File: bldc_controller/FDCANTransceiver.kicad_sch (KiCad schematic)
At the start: 4 parts, among them U9 TCAN1057AEVDRQ1

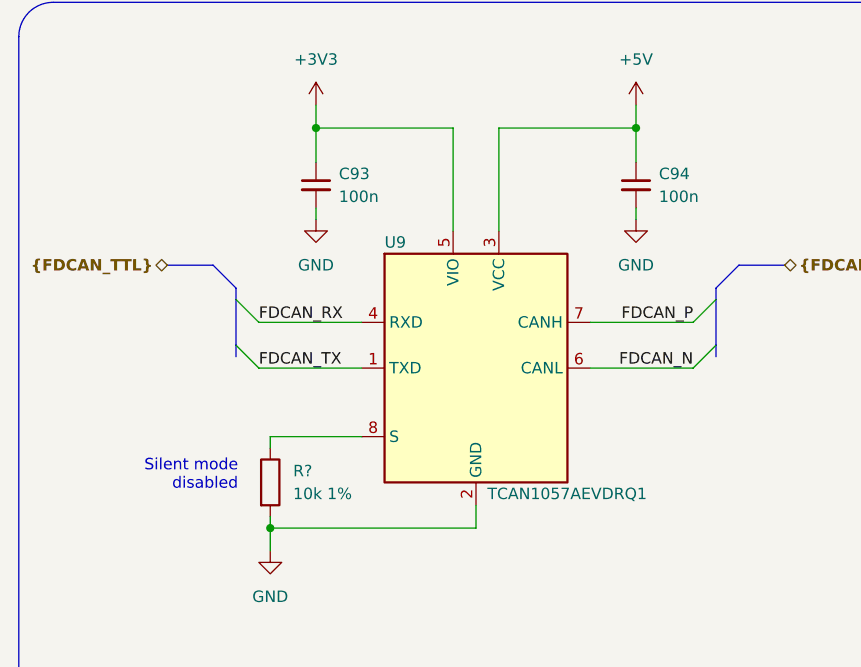
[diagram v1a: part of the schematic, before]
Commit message: added IPC-7351 compliant footprints and started routing
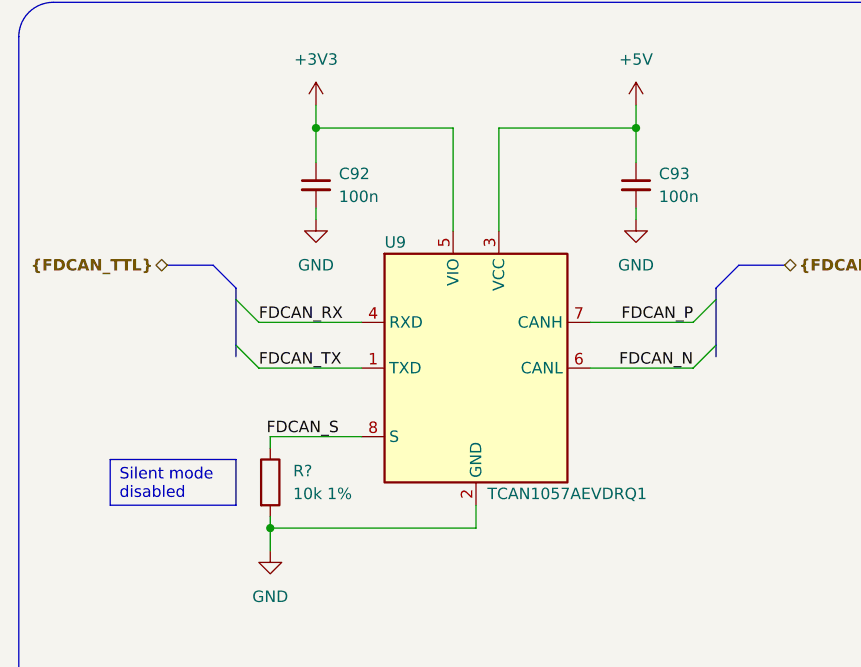
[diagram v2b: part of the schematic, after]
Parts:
- C92: renamed from C93; footprint Capacitor_SMD:C_0402_1005Metric -> 0_capacitor_smd:C_0402_1005_DensityHigh
- C93: renamed from C94; footprint Capacitor_SMD:C_0402_1005Metric -> 0_capacitor_smd:C_0402_1005_DensityHigh
- R?: footprint Resistor_SMD:R_0402_1005Metric -> 0_resistor_smd:R_0402_1005_DensityHigh
- U9: footprint Package_SO:SOIC-8-N7_3.9x4.9mm_P1.27mm -> Package_SO:SOIC-8_3.9x4.9mm_P1.27mm
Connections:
- net FDCAN_S: now reaches R?.1, U9.8 (S)
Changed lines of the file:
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@@
+    (stroke (width 0) (type default))
+  )
+  (wire (pts (xy 127 100.33) (xy 137.16 100.33))
     (stroke (width 0) (type default))
   )
@@
     (stroke (width 0) (type default))
   )
-  (wire (pts (xy 127 100.33) (xy 137.16 100.33))
-    (stroke (width 0) (type default))
-  )
   (wire (pts (xy 147.32 66.04) (xy 147.32 77.47))
     (stroke (width 0) (type default))
@@
     (stroke (width 0) (type default))
     (fill (type none))
-  )
-  (text_box "Silent mode disabled"
-    (at 110.49 101.6 0) (size 13.97 6.35)
-    (stroke (width -0.0001) (type default))
-    (fill (type none))
-    (effects (font (size 1.27 1.27)) (justify right top))
   )
   (text_box "Back to Top Level"
@@
     (effects (font (size 2.54 2.54) (color 0 0 0 1)) (justify bottom))
   )
+  (text_box "Silent mode disabled"
+    (at 109.22 102.87 0) (size 13.97 5.08)
+    (stroke (width 0) (type default) (color 0 0 0 1))
+    (fill (type color) (color 191 240 255 1))
+    (effects (font (size 1.27 1.27) (color 0 0 0 1)) (justify left))
+  )
+  (label "FDCAN_S" (at 134.62 100.33 180) (fields_autoplaced)
+    (effects (font (size 1.27 1.27)) (justify right bottom))
+  )
   (label "FDCAN_P" (at 173.99 87.63 180) (fields_autoplaced)
     (effects (font (size 1.27 1.27)) (justify right bottom))
@@
   (symbol (lib_id "power:+3V3") (at 132.08 63.5 0) (unit 1)
     (in_bom yes) (on_board yes) (dnp no) (fields_autoplaced)
-    (property "Reference" "#PWR054" (at 132.08 67.31 0)
+    (property "Reference" "#PWR053" (at 132.08 67.31 0)
       (effects (font (size 1.27 1.27)) hide)
     )
@@
       (project "bldc_controller"
         (path "/0650c7a8-acba-429c-9f8e-eec0baf0bc1c/926acdff-90be-4f7b-9e19-9f96ee9f0571"
+          (reference "#PWR053") (unit 1)
+        )
+      )
+    )
+  )
+  (symbol (lib_id "power:GND") (at 127 113.03 0) (unit 1)
+    (in_bom yes) (on_board yes) (dnp no) (fields_autoplaced)
+    (property "Reference" "#PWR052" (at 127 119.38 0)
+      (effects (font (size 1.27 1.27)) hide)
+    )
+    (property "Value" "GND" (at 127 118.11 0)
+      (effects (font (size 1.27 1.27)))
+    )
+    (property "Footprint" "" (at 127 113.03 0)
+      (effects (font (size 1.27 1.27)) hide)
+    )
+    (property "Datasheet" "" (at 127 113.03 0)
+      (effects (font (size 1.27 1.27)) hide)
+    )
+    (pin "1")
+    (instances
+      (project "bldc_controller"
+        (path "/0650c7a8-acba-429c-9f8e-eec0baf0bc1c/926acdff-90be-4f7b-9e19-9f96ee9f0571"
+          (reference "#PWR052") (unit 1)
+        )
+      )
+    )
+  )
+  (symbol (lib_id "power:GND") (at 132.08 76.2 0) (unit 1)
+    (in_bom yes) (on_board yes) (dnp no) (fields_autoplaced)
+    (property "Reference" "#PWR054" (at 132.08 82.55 0)
+      (effects (font (size 1.27 1.27)) hide)
+    )
+    (property "Value" "GND" (at 132.08 81.28 0)
+      (effects (font (size 1.27 1.27)))
+    )
+    (property "Footprint" "" (at 132.08 76.2 0)
+      (effects (font (size 1.27 1.27)) hide)
+    )
+    (property "Datasheet" "" (at 132.08 76.2 0)
+      (effects (font (size 1.27 1.27)) hide)
+    )
+    (pin "1")
+    (instances
+      (project "bldc_controller"
+        (path "/0650c7a8-acba-429c-9f8e-eec0baf0bc1c/926acdff-90be-4f7b-9e19-9f96ee9f0571"
           (reference "#PWR054") (unit 1)
         )
@@
     )
   )
-  (symbol (lib_id "power:GND") (at 127 113.03 0) (unit 1)
-    (in_bom yes) (on_board yes) (dnp no) (fields_autoplaced)
-    (property "Reference" "#PWR053" (at 127 119.38 0)
-      (effects (font (size 1.27 1.27)) hide)
-    )
-    (property "Value" "GND" (at 127 118.11 0)
-      (effects (font (size 1.27 1.27)))
-    )
-    (property "Footprint" "" (at 127 113.03 0)
-      (effects (font (size 1.27 1.27)) hide)
-    )
-    (property "Datasheet" "" (at 127 113.03 0)
-      (effects (font (size 1.27 1.27)) hide)
-    )
-    (pin "1")
-    (instances
-      (project "bldc_controller"
-        (path "/0650c7a8-acba-429c-9f8e-eec0baf0bc1c/926acdff-90be-4f7b-9e19-9f96ee9f0571"
-          (reference "#PWR053") (unit 1)
-        )
-      )
-    )
-  )
-  (symbol (lib_id "power:GND") (at 132.08 76.2 0) (unit 1)
-    (in_bom yes) (on_board yes) (dnp no) (fields_autoplaced)
-    (property "Reference" "#PWR055" (at 132.08 82.55 0)
-      (effects (font (size 1.27 1.27)) hide)
-    )
-    (property "Value" "GND" (at 132.08 81.28 0)
-      (effects (font (size 1.27 1.27)))
-    )
-    (property "Footprint" "" (at 132.08 76.2 0)
-      (effects (font (size 1.27 1.27)) hide)
-    )
-    (property "Datasheet" "" (at 132.08 76.2 0)
-      (effects (font (size 1.27 1.27)) hide)
-    )
-    (pin "1")
-    (instances
-      (project "bldc_controller"
-        (path "/0650c7a8-acba-429c-9f8e-eec0baf0bc1c/926acdff-90be-4f7b-9e19-9f96ee9f0571"
-          (reference "#PWR055") (unit 1)
-        )
-      )
-    )
-  )
   (symbol (lib_id "power:GND") (at 167.64 76.2 0) (mirror y) (unit 1)
     (in_bom yes) (on_board yes) (dnp no) (fields_autoplaced)
-    (property "Reference" "#PWR057" (at 167.64 82.55 0)
+    (property "Reference" "#PWR056" (at 167.64 82.55 0)
       (effects (font (size 1.27 1.27)) hide)
     )
@@
       (project "bldc_controller"
         (path "/0650c7a8-acba-429c-9f8e-eec0baf0bc1c/926acdff-90be-4f7b-9e19-9f96ee9f0571"
-          (reference "#PWR057") (unit 1)
+          (reference "#PWR056") (unit 1)
         )
       )
@@
   (symbol (lib_id "Device:C_Small") (at 167.64 72.39 0) (unit 1)
     (in_bom yes) (on_board yes) (dnp no)
-    (property "Reference" "C94" (at 170.18 71.1263 0)
+    (property "Reference" "C93" (at 170.18 71.1263 0)
       (effects (font (size 1.27 1.27)) (justify left))
     )
@@
       (effects (font (size 1.27 1.27)) (justify left))
     )
-    (property "Footprint" "Capacitor_SMD:C_0402_1005Metric" (at 167.64 72.39 0)
+    (property "Footprint" "0_capacitor_smd:C_0402_1005_DensityHigh" (at 167.64 72.39 0)
       (effects (font (size 1.27 1.27)) hide)
     )
@@
       (project "bldc_controller"
         (path "/0650c7a8-acba-429c-9f8e-eec0baf0bc1c/926acdff-90be-4f7b-9e19-9f96ee9f0571"
-          (reference "C94") (unit 1)
+          (reference "C93") (unit 1)
         )
       )
@@
   (symbol (lib_id "power:+5V") (at 167.64 63.5 0) (unit 1)
     (in_bom yes) (on_board yes) (dnp no) (fields_autoplaced)
-    (property "Reference" "#PWR056" (at 167.64 67.31 0)
+    (property "Reference" "#PWR055" (at 167.64 67.31 0)
       (effects (font (size 1.27 1.27)) hide)
     )
@@
       (project "bldc_controller"
         (path "/0650c7a8-acba-429c-9f8e-eec0baf0bc1c/926acdff-90be-4f7b-9e19-9f96ee9f0571"
-          (reference "#PWR056") (unit 1)
+          (reference "#PWR055") (unit 1)
         )
       )
@@
       (effects (font (size 1.27 1.27)) (justify left))
     )
-    (property "Footprint" "Package_SO:SOIC-8-N7_3.9x4.9mm_P1.27mm" (at 149.86 116.84 0)
+    (property "Footprint" "Package_SO:SOIC-8_3.9x4.9mm_P1.27mm" (at 149.86 116.84 0)
       (effects (font (size 1.27 1.27)) hide)
     )
@@
   (symbol (lib_id "Device:C_Small") (at 132.08 72.39 0) (unit 1)
     (in_bom yes) (on_board yes) (dnp no) (fields_autoplaced)
-    (property "Reference" "C93" (at 134.62 71.1263 0)
+    (property "Reference" "C92" (at 134.62 71.1263 0)
       (effects (font (size 1.27 1.27)) (justify left))
     )
@@
       (effects (font (size 1.27 1.27)) (justify left))
     )
-    (property "Footprint" "Capacitor_SMD:C_0402_1005Metric" (at 132.08 72.39 0)
+    (property "Footprint" "0_capacitor_smd:C_0402_1005_DensityHigh" (at 132.08 72.39 0)
       (effects (font (size 1.27 1.27)) hide)
     )
@@
       (project "bldc_controller"
         (path "/0650c7a8-acba-429c-9f8e-eec0baf0bc1c/926acdff-90be-4f7b-9e19-9f96ee9f0571"
-          (reference "C93") (unit 1)
+          (reference "C92") (unit 1)
         )
       )
@@
       (effects (font (size 1.27 1.27)) (justify left))
     )
-    (property "Footprint" "Resistor_SMD:R_0402_1005Metric" (at 125.222 105.41 90)
-      (effects (font (size 1.27 1.27)) hide)
-    )
+    (property "Footprint" "0_resistor_smd:R_0402_1005_DensityHigh" (at 125.222 105.41 90)
+      (effects (font (size 1.27 1.27)) hide)
+    )

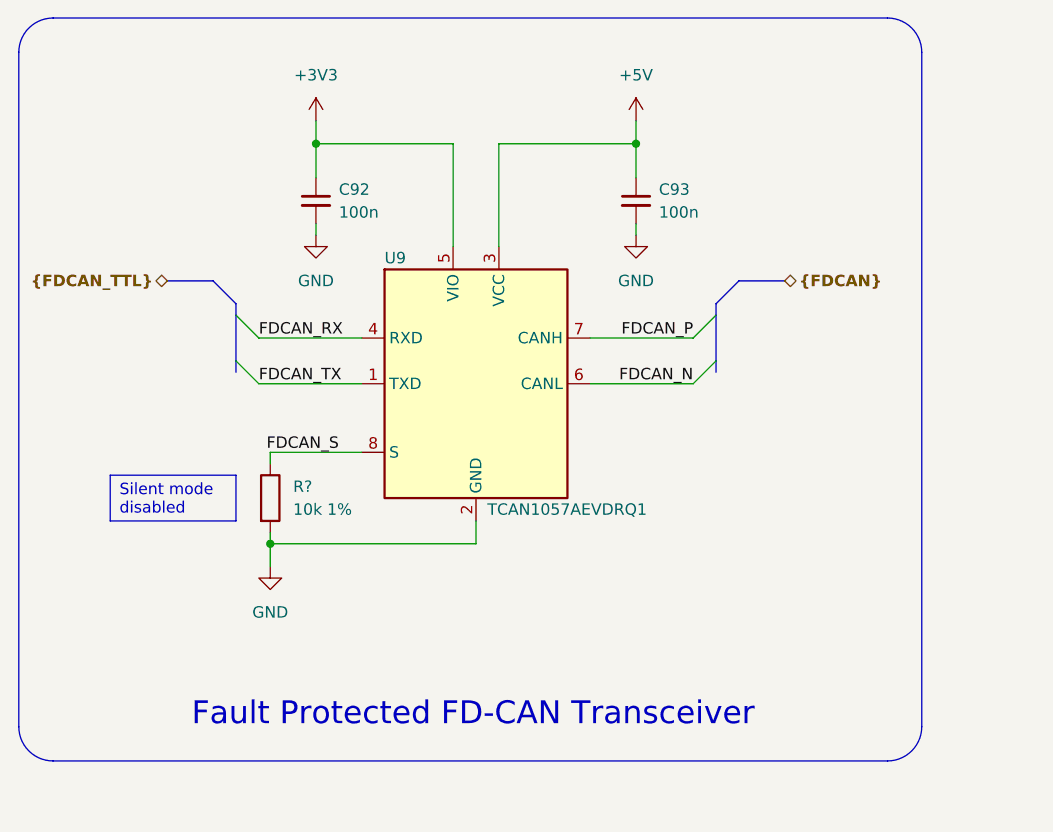
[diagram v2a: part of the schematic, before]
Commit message: routed CAN, added new footprints
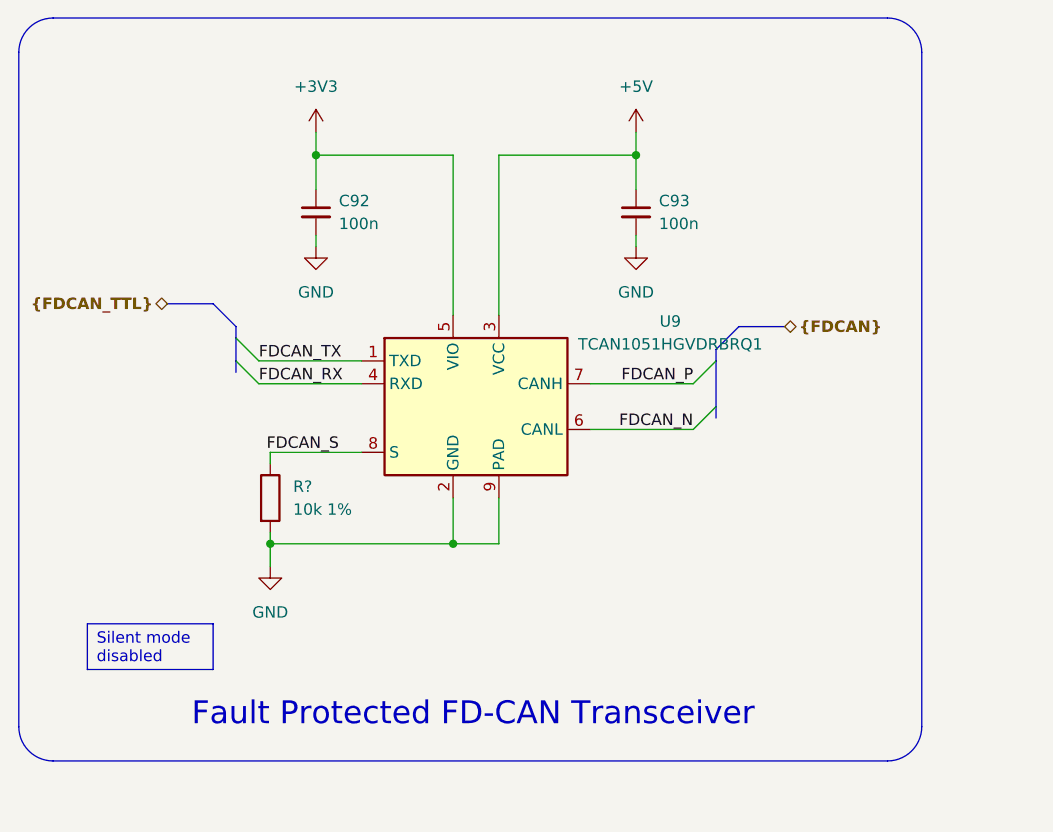
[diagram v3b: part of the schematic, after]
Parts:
- removed U9: TCAN1057AEVDRQ1, Package_SO:SOIC-8_3.9x4.9mm_P1.27mm, symbol 0_transceiver:TCAN1057AEVDRQ1
- added U9: TCAN1051HGVDRBRQ1, 0_package_SON:HVSON-8-1EP_3x3mm_P0.65mm_EP1.6x2.4mm_ThermalVias, symbol 0_interface_can:TCAN1051HGVDRBRQ1
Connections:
- net +3V3: now also U9.5 (VIO)
- net +5V: now also U9.3 (VCC)
- net FDCAN_N: now also U9.6 (CANL)
- net FDCAN_P: now also U9.7 (CANH)
- net FDCAN_RX: now also U9.4 (RXD)
- net FDCAN_S: now also U9.8 (S)
- net FDCAN_TX: now also U9.1 (TXD)
- net GND: now also U9.2 (GND), U9.9 (PAD)
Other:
- moved on the sheet: C92, C93

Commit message: minor changes before changing mcu
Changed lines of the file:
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@@
   )
   (symbol (lib_id "0_interface_can:TCAN1051HGVDRBRQ1") (at 149.86 95.25 0) (unit 1)
-    (in_bom yes) (on_board yes) (dnp no) (fields_autoplaced)
-    (property "Reference" "U9" (at 171.45 85.7819 0)
-      (effects (font (size 1.27 1.27)))
+    (in_bom yes) (on_board yes) (dnp no)
+    (property "Reference" "U9" (at 153.67 105.41 0)
+      (effects (font (size 1.27 1.27)) (justify left))
     )
-    (property "Value" "TCAN1051HGVDRBRQ1" (at 171.45 88.3219 0)
-      (effects (font (size 1.27 1.27)))
+    (property "Value" "TCAN1051HGVDRBRQ1" (at 153.67 107.95 0)
+      (effects (font (size 1.27 1.27)) (justify left))
     )
     (property "Footprint" "0_package_SON:HVSON-8-1EP_3x3mm_P0.65mm_EP1.6x2.4mm_ThermalVias" (at 148.59 119.38 0)
